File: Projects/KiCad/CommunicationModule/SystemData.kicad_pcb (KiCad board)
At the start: 2 copper layers, 110 x 95 mm, 37 parts, among them J1 Conn_01x08, SW1 SW_Push, U1 MCP2562-E-P, U2 MCP2515-I/P, U3 NJM7805SDL1, U4 ABX00012, Y1 8MHz

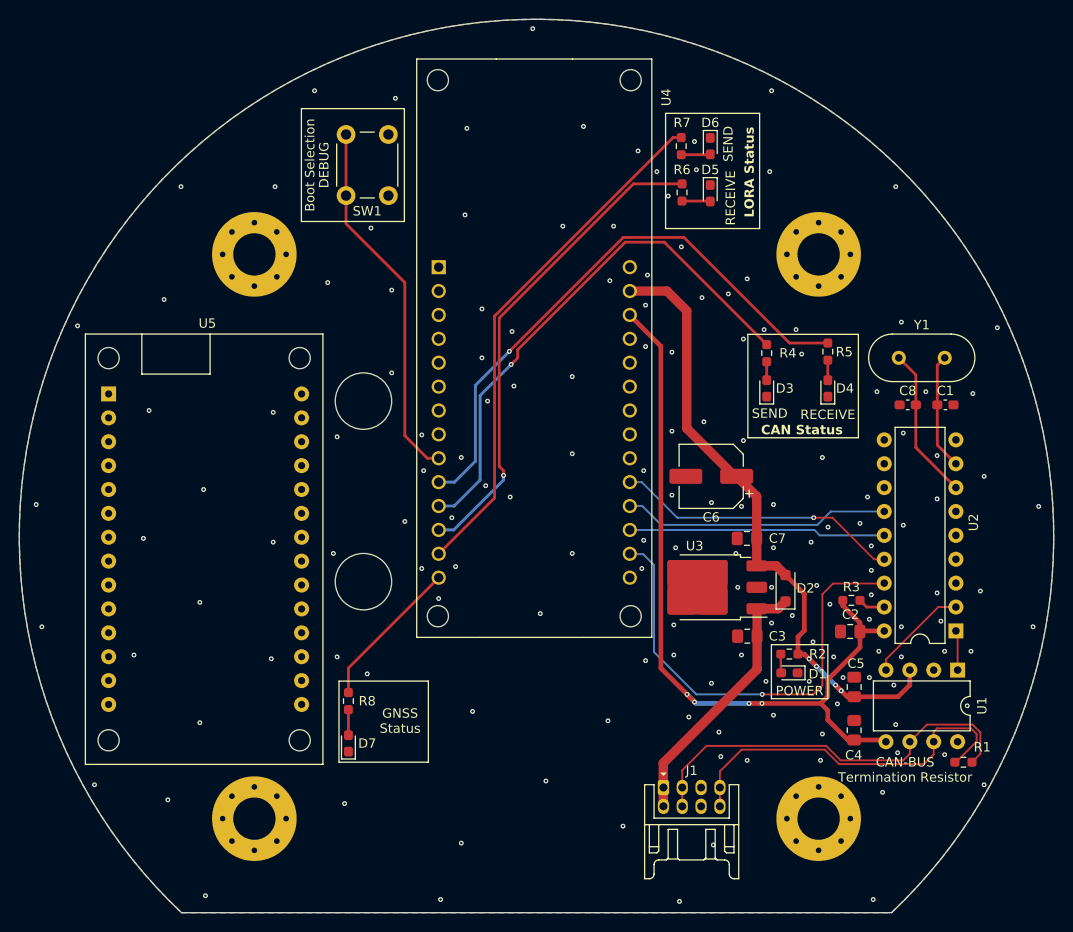
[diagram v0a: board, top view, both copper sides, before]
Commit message: 穴径を調整
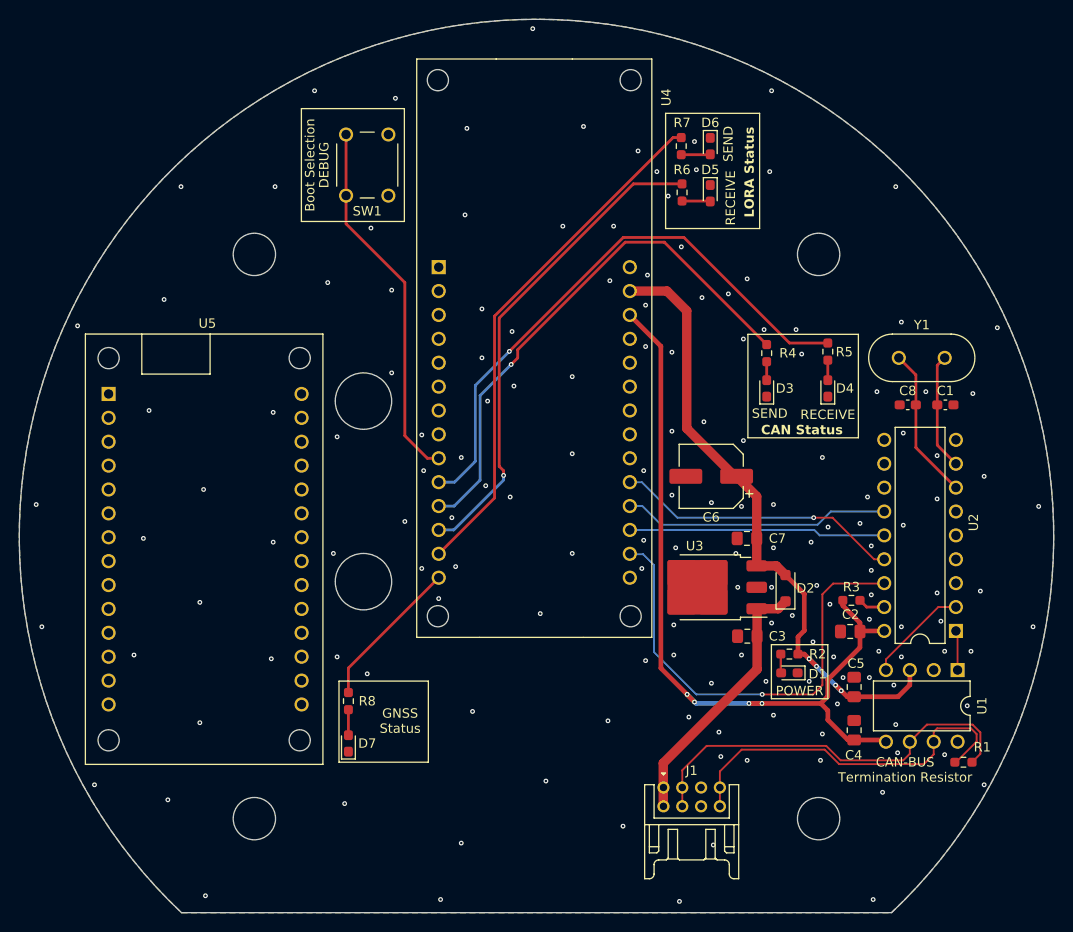
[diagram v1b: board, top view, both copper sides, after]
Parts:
- REF** (x4): value MountingHole_4.5mm_Pad_Via -> MountingHole_4.5mm; footprint MountingHole:MountingHole_4.5mm_Pad_Via -> MountingHole:MountingHole_4.5mm

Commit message: テストポイントを追加
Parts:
- added TP1: TestPoint, Connector_Pin:Pin_D1.0mm_L10.0mm, F.Cu at (172.1, 128.9)
- added TP2: TestPoint, Connector_Pin:Pin_D1.0mm_L10.0mm, F.Cu at (172.1, 125.7)
- J1: footprint Hirose_Connector:Hirose_DF11B-8DP-2DS -> Connector_Hirose:Hirose_DF11-8DP-2DSA_2x04_P2.00mm_Vertical
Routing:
- net CAN_H: track 39.8 -> 38.6 mm
- net CAN_L: track 43.5 -> 44.4 mm
- net GND: vias 158 -> 156
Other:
- board text added: "3.3V"
- board text added: "5V IN"
- board text added: "CAN H"
- board text added: "CAN L"
- board text added: "MCP"
- board text added: "MOSI"
- board text added: "SCLK"

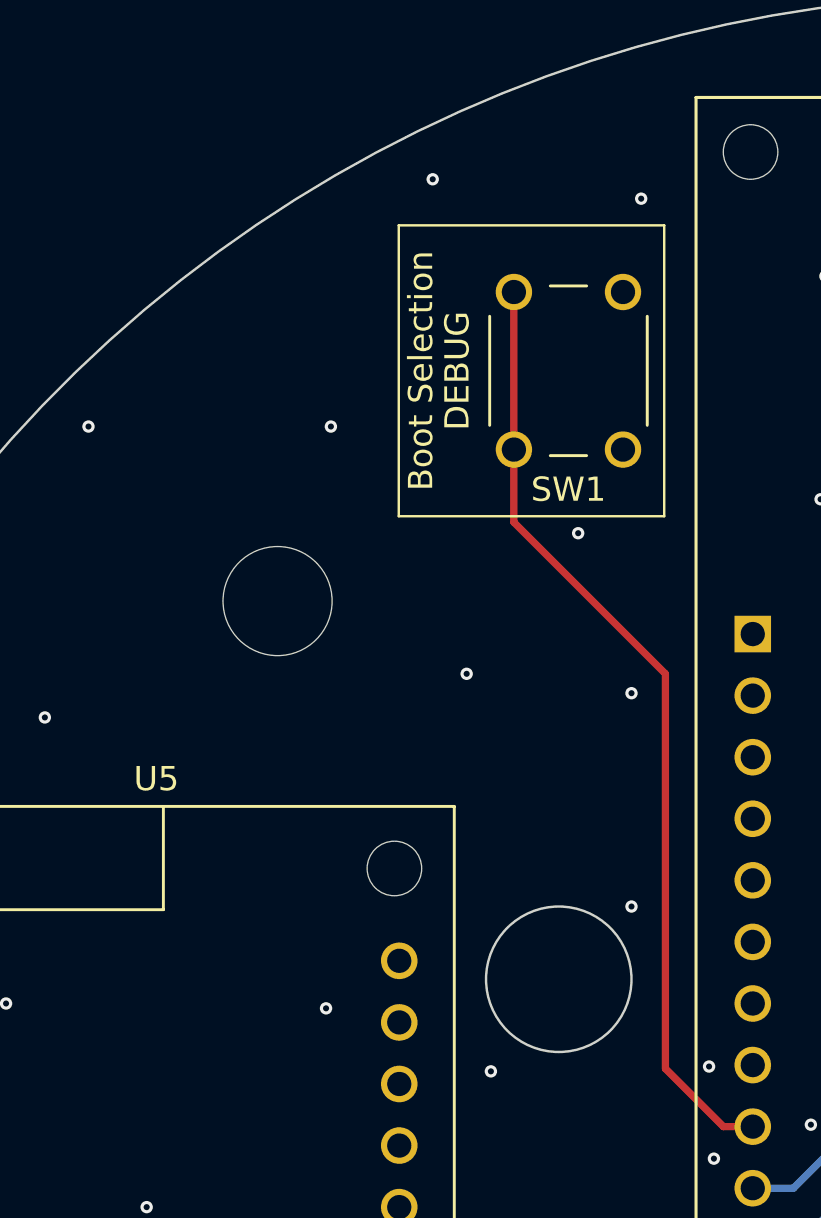
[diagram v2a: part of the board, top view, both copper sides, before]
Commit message: スイッチをピアノスイッチに変更
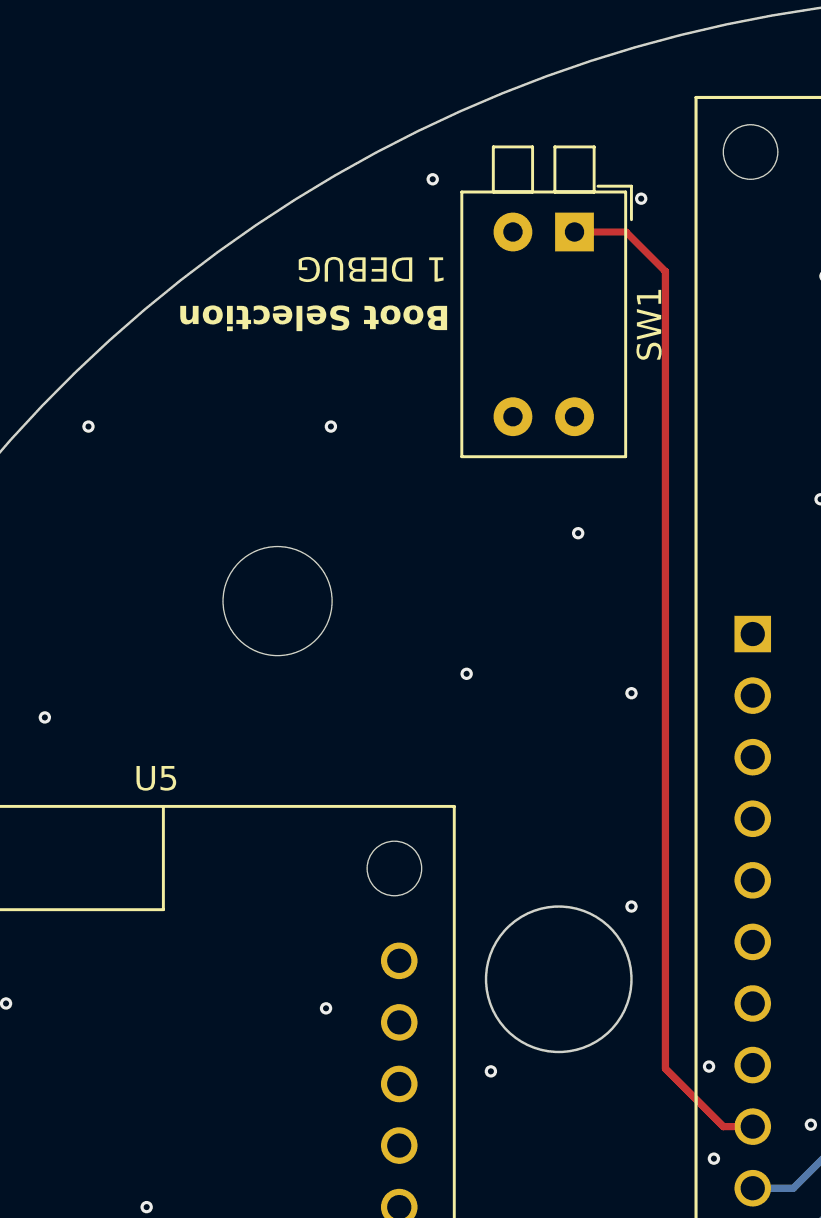
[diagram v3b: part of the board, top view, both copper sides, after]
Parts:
- SW1: value SW_Push -> SW_DIP_x02; footprint Button_Switch_THT:SW_PUSH_6mm -> Button_Switch_THT:SW_DIP_SPSTx02_Piano_10.8x6.64mm_W7.62mm_P2.54mm
- moved SW1 3.18 mm to (130.8, 59.8)
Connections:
- SW1 pad 1: GND -> DEBUG_MODE
- SW1 pad 2: DEBUG_MODE -> (no net)
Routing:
- net DEBUG_MODE: track 39.2 -> 41.9 mm
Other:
- board text added: "1 DEBUG"
- board text removed: "DEBUG"

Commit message: ベタを修正
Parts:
- moved C6 5.52 mm to (172.6, 98.5), turned to 0 degrees
- moved C7 1.60 mm to (171.0, 106.8)
- moved C3 1.40 mm to (169.7, 116.3)
- moved U3 1.23 mm to (167.2, 111.6)
- moved D2 1.18 mm to (175.4, 111.6)
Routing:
- net +5V: track 67.9 -> 70.1 mm
- net +12V: track 28.5 -> 27.6 mm
- net GND: vias 156 -> 150

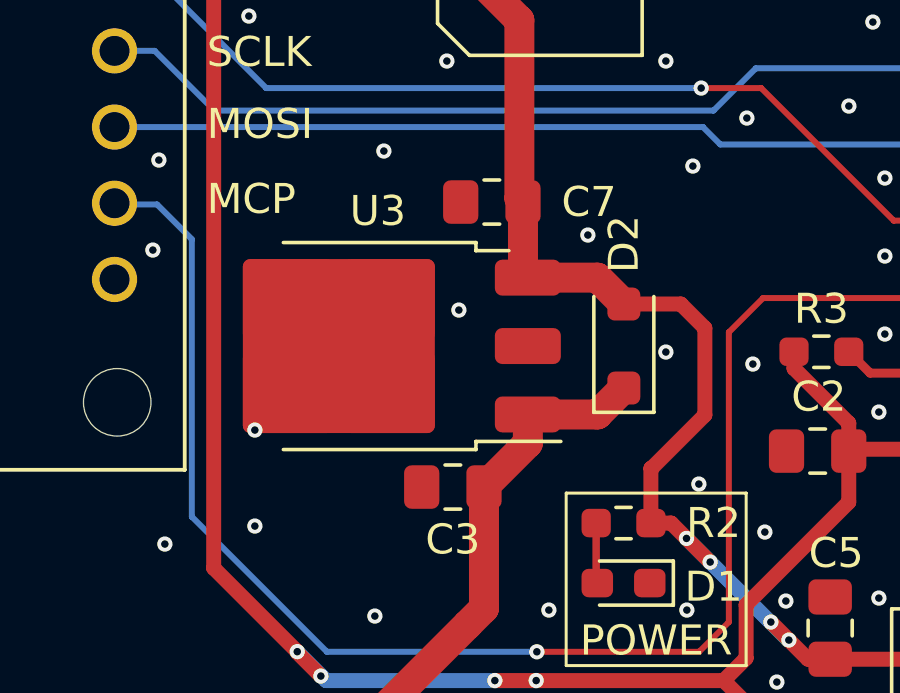
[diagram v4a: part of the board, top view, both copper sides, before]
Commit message: 三端子レギュレータをTO-252-3からTO-252-2に変更
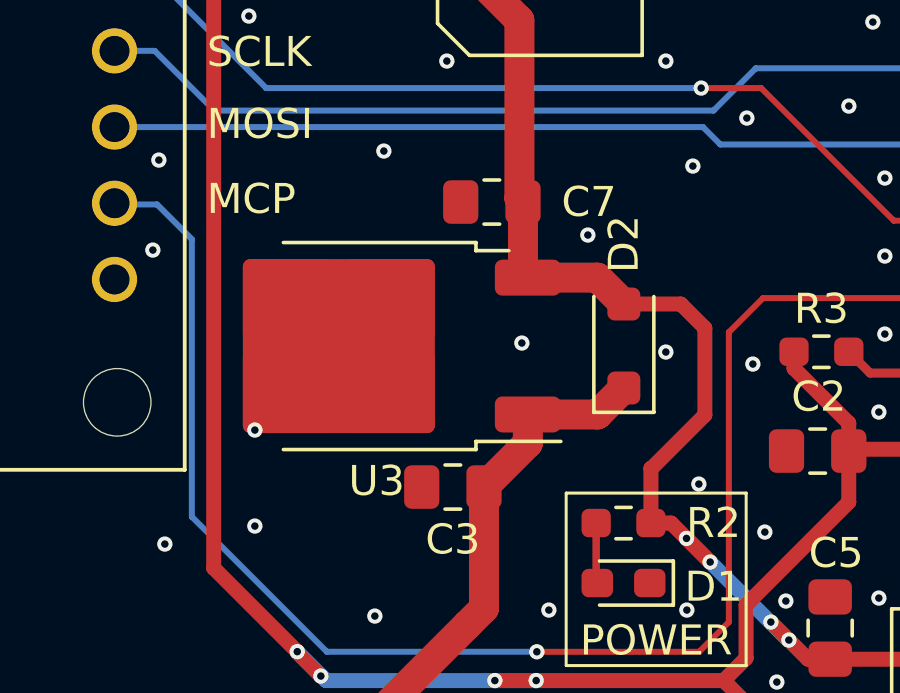
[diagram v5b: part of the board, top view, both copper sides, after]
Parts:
- U3: footprint Package_TO_SOT_SMD:TO-252-3_TabPin2 -> Package_TO_SOT_SMD:TO-252-2
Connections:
- SW1 pad 2: (no net) -> unconnected-(SW1-Pad2)
- SW1 pad 3: GND -> unconnected-(SW1-Pad3)
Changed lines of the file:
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@@
   (net 77 "unconnected-(U5-Pad27)")
   (net 78 "+12V")
+  (net 79 "unconnected-(SW1-Pad2)")
+  (net 80 "unconnected-(SW1-Pad3)")
   (footprint "MountingHole:MountingHole_4.5mm" locked (layer "F.Cu")
     (at 178.5 75)
@@
     )
   )
-  (footprint "Package_TO_SOT_SMD:TO-252-3_TabPin2" (layer "F.Cu")
+  (footprint "Package_TO_SOT_SMD:TO-252-2" (layer "F.Cu")
     (at 167.16 111.599432 180)
     (descr "TO-252/DPAK SMD package, http://www.infineon.com/cms/en/product/packages/PG-TO252/PG-TO252-3-1/")
@@
     (property "ki_keywords" "Voltage Regulator 1.5A Positive")
     (attr smd)
-    (fp_text reference "U3" (at -0.04 4.5) (layer "F.SilkS")
+    (fp_text reference "U3" (at 0 -4.5 180) (layer "F.SilkS")
         (effects (font (size 1 1) (thickness 0.15)))
     )
-    (fp_text value "NJM7805SDL1" (at 0 4.5) (layer "F.Fab")
+    (fp_text value "NJM7805SDL1" (at 0 4.5 180) (layer "F.Fab")
         (effects (font (size 1 1) (thickness 0.15)))
     )
-    (fp_text user "${REFERENCE}" (at 0 0) (layer "F.Fab")
+    (fp_text user "${REFERENCE}" (at 0 0 180) (layer "F.Fab")
         (effects (font (size 1 1) (thickness 0.15)))
     )
@@
     (fp_line (start -5.81 -1.905) (end -3.11 -1.905)
       (stroke (width 0.1) (type solid)) (layer "F.Fab"))
-    (fp_line (start -5.81 -0.375) (end -5.81 0.375)
-      (stroke (width 0.1) (type solid)) (layer "F.Fab"))
-    (fp_line (start -5.81 0.375) (end -3.11 0.375)
-      (stroke (width 0.1) (type solid)) (layer "F.Fab"))
     (fp_line (start -5.81 1.905) (end -5.81 2.655)
       (stroke (width 0.1) (type solid)) (layer "F.Fab"))
@@
     (fp_line (start -3.11 -2.25) (end -2.11 -3.25)
       (stroke (width 0.1) (type solid)) (layer "F.Fab"))
-    (fp_line (start -3.11 -0.375) (end -5.81 -0.375)
-      (stroke (width 0.1) (type solid)) (layer "F.Fab"))
     (fp_line (start -3.11 1.905) (end -5.81 1.905)
       (stroke (width 0.1) (type solid)) (layer "F.Fab"))
@@
     (pad "1" smd roundrect (at -5.04 -2.28 180) (size 2.2 1.2) (layers "F.Cu" "F.Paste" "F.Mask") (roundrect_rratio 0.208333)
       (net 78 "+12V") (pinfunction "IN") (pintype "power_in"))
-    (pad "2" smd roundrect (at -5.04 0 180) (size 2.2 1.2) (layers "F.Cu" "F.Paste" "F.Mask") (roundrect_rratio 0.208333)
-      (net 2 "GND") (pinfunction "GND") (pintype "power_in"))
     (pad "2" smd roundrect (at -0.415 -1.525 180) (size 3.05 2.75) (layers "F.Cu" "F.Paste") (roundrect_rratio 0.090909)
       (net 2 "GND") (pinfunction "GND") (pintype "power_in"))
@@
     (pad "3" smd roundrect (at -5.04 2.28 180) (size 2.2 1.2) (layers "F.Cu" "F.Paste" "F.Mask") (roundrect_rratio 0.208333)
       (net 3 "+5V") (pinfunction "OUT") (pintype "power_out"))
-    (model "${KICAD6_3DMODEL_DIR}/Package_TO_SOT_SMD.3dshapes/TO-252-3_TabPin2.wrl"
+    (model "${KICAD6_3DMODEL_DIR}/Package_TO_SOT_SMD.3dshapes/TO-252-2.wrl"
       (offset (xyz 0 0 0))
       (scale (xyz 1 1 1))
@@
     (descr "2x-dip-switch SPST , Piano, row spacing 7.62 mm (300 mils), body size 10.8x6.64mm")
     (tags "DIP Switch SPST Piano 7.62mm 300mil")
-    (property "Sheetfile" "SensingModule.kicad_sch")
+    (property "Sheetfile" "SystemData.kicad_sch")
     (property "Sheetname" "")
     (property "ki_description" "2x DIP Switch, Single Pole Single Throw (SPST) switch, small symbol")
@@
       (net 74 "DEBUG_MODE") (pintype "passive"))
     (pad "2" thru_hole oval (at 0 2.54 270) (size 1.6 1.6) (drill 0.8) (layers "*.Cu" "*.Mask")
-      (pintype "passive"))
+      (net 79 "unconnected-(SW1-Pad2)") (pintype "passive"))
     (pad "3" thru_hole oval (at 7.62 2.54 270) (size 1.6 1.6) (drill 0.8) (layers "*.Cu" "*.Mask")
-      (net 2 "GND") (pintype "passive"))
+      (net 80 "unconnected-(SW1-Pad3)") (pintype "passive"))
     (pad "4" thru_hole oval (at 7.62 0 270) (size 1.6 1.6) (drill 0.8) (layers "*.Cu" "*.Mask")
       (net 2 "GND") (pintype "passive"))
@@
   (via (at 186.7 67.8) (size 0.51) (drill 0.25) (layers "F.Cu" "B.Cu") (free) (net 2))
   (via (at 142.7 80.8) (size 0.51) (drill 0.25) (layers "F.Cu" "B.Cu") (free) (net 2))
-  (via (at 169.9 110.4) (size 0.51) (drill 0.25) (layers "F.Cu" "B.Cu") (free) (net 2))
+  (via (at 172 111.499432) (size 0.51) (drill 0.25) (layers "F.Cu" "B.Cu") (free) (net 2))
   (via (at 146.1 89) (size 0.51) (drill 0.25) (layers "F.Cu" "B.Cu") (free) (net 2))
   (via (at 162.5 68.8) (size 0.51) (drill 0.25) (layers "F.Cu" "B.Cu") (free) (net 2))

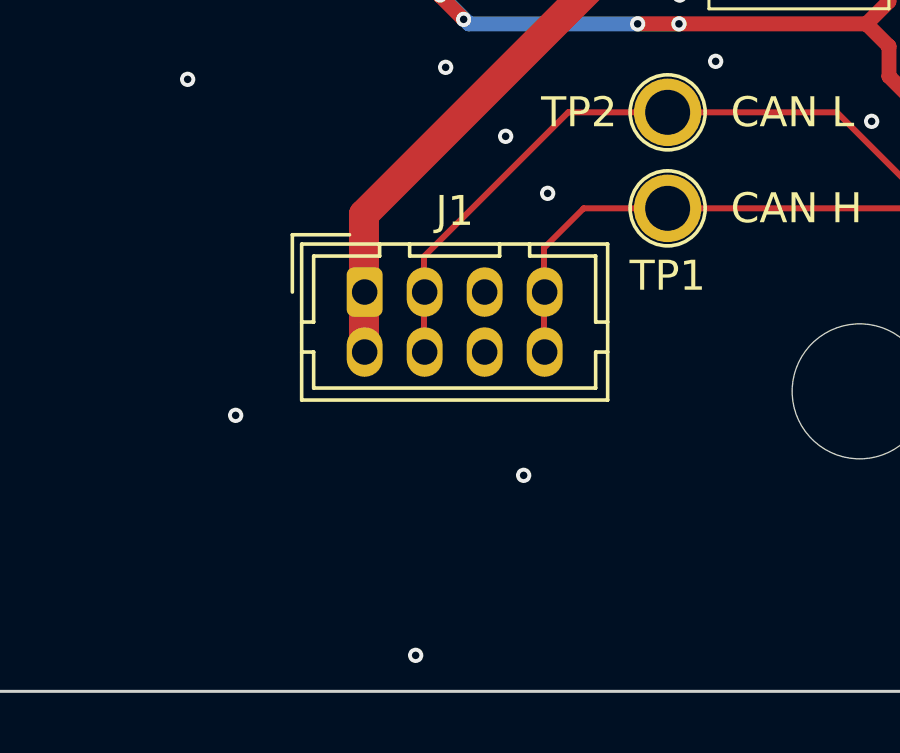
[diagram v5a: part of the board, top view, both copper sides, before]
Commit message: STEPファイルを再生成
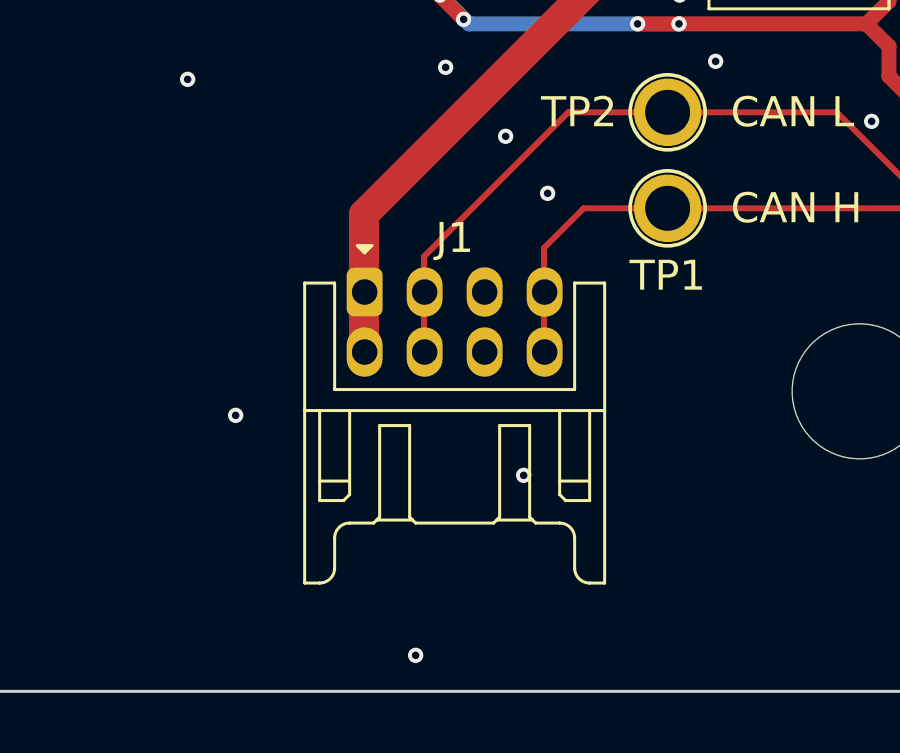
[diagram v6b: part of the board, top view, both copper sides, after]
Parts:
- J1: footprint Connector_Hirose:Hirose_DF11-8DP-2DSA_2x04_P2.00mm_Vertical -> Hirose_Connector:Hirose_DF11B-8DP-2DS
